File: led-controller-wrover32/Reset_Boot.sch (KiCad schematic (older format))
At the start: 8 parts, among them Q5 BSS138DW-7-F, SW1 SW_SPST_KMR2, SW2 SW_SPST_KMR2

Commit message: Cleanup
Signed-off-by: Aaron Williams <aaron.w2@gmail.com>
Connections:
- net ~RST_SW_OUT: now reaches C23.1, R3.1, RN6.2 (R2.1), RN6.3 (R3.1), RN6.4 (R4.1), SW2.2 (S1)
- net RST_IO2_DRV: now reaches Q5.2 (G2), RN6.7 (R2.2)
- net RST_IO0_DRV: now reaches Q5.5 (G1), RN6.6 (R3.2)
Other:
- moved on the sheet: Q5
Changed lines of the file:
@@
 EESchema Schematic File Version 4
-LIBS:led-controller-wrover32-cache
 EELAYER 30 0
 EELAYER END
 $Descr A4 11693 8268
 encoding utf-8
-Sheet 4 4
+Sheet 4 5
 Title ""
 Date ""
@@
 L dk_Transistors-FETs-MOSFETs-Arrays:BSS138DW-7-F Q5
 U 1 1 5DD66E94
-P 4800 2350
-F 0 "Q5" H 4750 2837 60  0000 C CNN
-F 1 "BSS138DW-7-F" H 4750 2731 60  0000 C CNN
-F 2 "Package_TO_SOT_SMD:SOT-363_SC-70-6" H 5000 2550 60  0001 L CNN
-F 3 "https://www.diodes.com/assets/Datasheets/ds30203.pdf" V 5000 2650 60  0001 L CNN
-F 4 "BSS138DW-FDICT-ND" H 5000 2750 60  0001 L CNN "Digi-Key_PN"
-F 5 "BSS138DW-7-F" H 5000 2850 60  0001 L CNN "MPN"
-F 6 "Discrete Semiconductor Products" H 5000 2950 60  0001 L CNN "Category"
-F 7 "Transistors - FETs, MOSFETs - Arrays" H 5000 3050 60  0001 L CNN "Family"
-F 8 "https://www.diodes.com/assets/Datasheets/ds30203.pdf" H 5000 3150 60  0001 L CNN "DK_Datasheet_Link"
-F 9 "/product-detail/en/diodes-incorporated/BSS138DW-7-F/BSS138DW-FDICT-ND/808541" H 5000 3250 60  0001 L CNN "DK_Detail_Page"
-F 10 "MOSFET 2N-CH 50V 0.2A SC70-6" H 5000 3350 60  0001 L CNN "Description"
-F 11 "Diodes Incorporated" H 5000 3450 60  0001 L CNN "Manufacturer"
-F 12 "Active" H 5000 3550 60  0001 L CNN "Status"
-F 13 "Diodes Incorporated" H 4800 2350 50  0001 C CNN "MFR"
-F 14 "Digikey" H 4800 2350 50  0001 C CNN "SPR"
-F 15 "BSS138DW-FDICT-ND" H 4800 2350 50  0001 C CNN "SPN"
-F 16 "https://www.digikey.com/products/en/discrete-semiconductor-products/transistors-fets-mosfets-arrays/289?k=BSS138DW-7-F&k=&pkeyword=BSS138DW-7-F&sv=0&pv7=2&sf=0&quantity=&ColumnSort=0&page=1&stock=1&nstock=1&pageSize=500" H 4800 2350 50  0001 C CNN "SPURL"
-	1    4800 2350
+P 5050 2350
+F 0 "Q5" H 5000 2837 60  0000 C CNN
+F 1 "BSS138DW-7-F" H 5000 2731 60  0000 C CNN
+F 2 "Package_TO_SOT_SMD:SOT-363_SC-70-6" H 5250 2550 60  0001 L CNN
+F 3 "https://www.diodes.com/assets/Datasheets/ds30203.pdf" V 5250 2650 60  0001 L CNN
+F 4 "BSS138DW-FDICT-ND" H 5250 2750 60  0001 L CNN "Digi-Key_PN"
+F 5 "BSS138DW-7-F" H 5250 2850 60  0001 L CNN "MPN"
+F 6 "Discrete Semiconductor Products" H 5250 2950 60  0001 L CNN "Category"
+F 7 "Transistors - FETs, MOSFETs - Arrays" H 5250 3050 60  0001 L CNN "Family"
+F 8 "https://www.diodes.com/assets/Datasheets/ds30203.pdf" H 5250 3150 60  0001 L CNN "DK_Datasheet_Link"
+F 9 "/product-detail/en/diodes-incorporated/BSS138DW-7-F/BSS138DW-FDICT-ND/808541" H 5250 3250 60  0001 L CNN "DK_Detail_Page"
+F 10 "MOSFET 2N-CH 50V 0.2A SC70-6" H 5250 3350 60  0001 L CNN "Description"
+F 11 "Diodes Incorporated" H 5250 3450 60  0001 L CNN "Manufacturer"
+F 12 "Active" H 5250 3550 60  0001 L CNN "Status"
+F 13 "Diodes Incorporated" H 5050 2350 50  0001 C CNN "MFR"
+F 14 "Digikey" H 5050 2350 50  0001 C CNN "SPR"
+F 15 "BSS138DW-FDICT-ND" H 5050 2350 50  0001 C CNN "SPN"
+F 16 "https://www.digikey.com/products/en/discrete-semiconductor-products/transistors-fets-mosfets-arrays/289?k=BSS138DW-7-F&k=&pkeyword=BSS138DW-7-F&sv=0&pv7=2&sf=0&quantity=&ColumnSort=0&page=1&stock=1&nstock=1&pageSize=500" H 5050 2350 50  0001 C CNN "SPURL"
+	1    5050 2350
 	1    0    0    -1
 $EndComp
@@
 $EndComp
 Wire Wire Line
-	4100 2450 4500 2450
+	4100 2450 4750 2450
 Wire Wire Line
 	4100 2350 4250 2350
@@
 	4250 2350 4250 1800
 Wire Wire Line
-	4250 1800 5200 1800
-Wire Wire Line
-	5200 1800 5200 2450
-Wire Wire Line
-	5200 2450 5000 2450
+	4250 1800 5450 1800
+Wire Wire Line
+	5450 1800 5450 2450
+Wire Wire Line
+	5450 2450 5250 2450
 $Comp
 L power:GND #PWR0127
 U 1 1 5DD73FDE
-P 4500 2150
-F 0 "#PWR0127" H 4500 1900 50  0001 C CNN
-F 1 "GND" H 4505 1977 50  0000 C CNN
-F 2 "" H 4500 2150 50  0001 C CNN
-F 3 "" H 4500 2150 50  0001 C CNN
-	1    4500 2150
+P 4750 2150
+F 0 "#PWR0127" H 4750 1900 50  0001 C CNN
+F 1 "GND" H 4755 1977 50  0000 C CNN
+F 2 "" H 4750 2150 50  0001 C CNN
+F 3 "" H 4750 2150 50  0001 C CNN
+	1    4750 2150
 	1    0    0    -1
 $EndComp
@@
 L power:GND #PWR0128
 U 1 1 5DD74502
-P 5000 2750
-F 0 "#PWR0128" H 5000 2500 50  0001 C CNN
-F 1 "GND" H 5005 2577 50  0000 C CNN
-F 2 "" H 5000 2750 50  0001 C CNN
-F 3 "" H 5000 2750 50  0001 C CNN
-	1    5000 2750
-	1    0    0    -1
-$EndComp
-Wire Wire Line
-	5000 2150 5650 2150
+P 5250 2750
+F 0 "#PWR0128" H 5250 2500 50  0001 C CNN
+F 1 "GND" H 5255 2577 50  0000 C CNN
+F 2 "" H 5250 2750 50  0001 C CNN
+F 3 "" H 5250 2750 50  0001 C CNN
+	1    5250 2750
+	1    0    0    -1
+$EndComp
+Wire Wire Line
+	5250 2150 5650 2150
 Text Label 5500 2150 0    50   ~ 0
 IO0
 Wire Wire Line
-	4500 2750 4500 3100
-Wire Wire Line
-	4500 3100 5650 3100
+	4750 2750 4750 3100
+Wire Wire Line
+	4750 3100 5650 3100
 Text Label 5500 3100 0    50   ~ 0
 IO2
@@
 NoConn ~ 4100 2250
 NoConn ~ 3700 2250
+Text Label 3200 2450 0    50   ~ 0
+~RST_SW_OUT
+Text Label 4450 1800 0    50   ~ 0
+RST_IO2_DRV
+Text Label 4150 2450 0    50   ~ 0
+RST_IO0_DRV
 $EndSCHEMATC

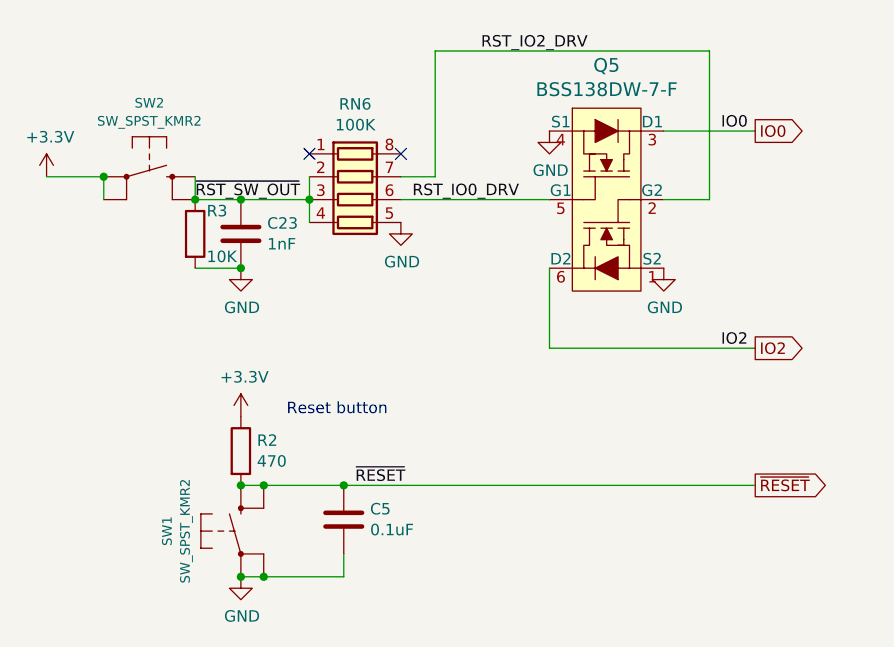
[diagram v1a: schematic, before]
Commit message: Fix reset circuit and other stuff
This fixes the reset circuit and moves a few components.  It also
cleans up the BOM a bit.

Also bumped to version 3.5.0

Signed-off-by: Aaron Williams <aaron.w2@gmail.com>
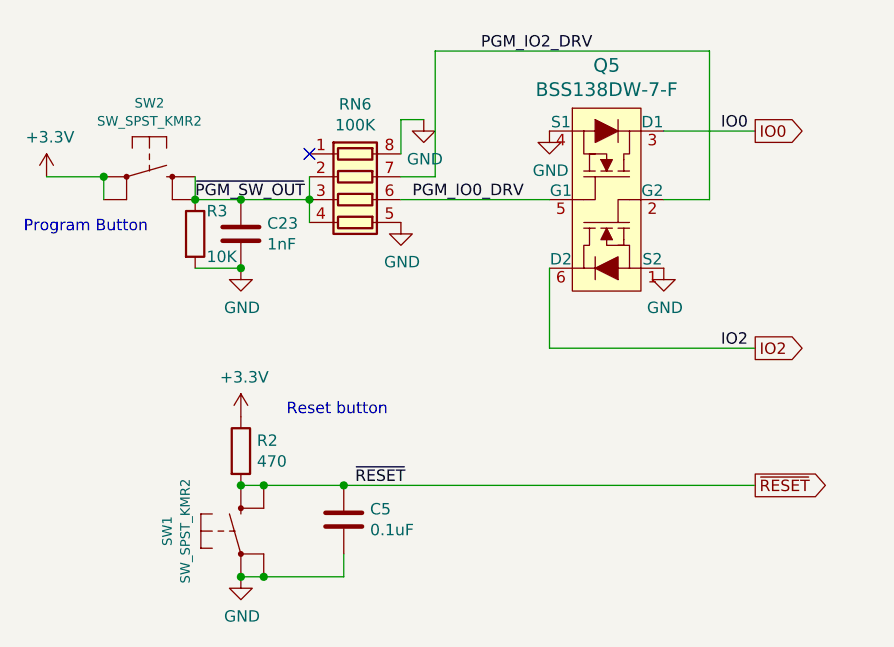
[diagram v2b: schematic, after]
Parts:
- R3: MFR (none) -> Vishay Dale; MPN (none) -> CRCW060310K0FKEC; SPN (none) -> 541-2979-1-ND; SPR (none) -> Digikey; SPURL (none) -> -
- RN6: MFR Bourns -> Panasonic; MPN CAT16-1003F4LF -> EXB-V8V103JV; SPN CAT16-1003F4LFCT-ND -> Y4103CT-ND
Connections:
- net GND: now also RN6.8 (R1.2)
- net RST_IO0_DRV renamed PGM_IO0_DRV
- net RST_IO2_DRV renamed PGM_IO2_DRV
- net ~RST_SW_OUT renamed ~PGM_SW_OUT
- no-connect marks 2 -> 1
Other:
- note added: "Program Button"

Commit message: Moved WS2813B after fixing footprint  v3.6
Signed-off-by: Aaron Williams <aaron.w2@gmail.com>
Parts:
- C23: value 1nF -> 22nF; MFR Kemet -> Yageo; MPN C0603C102K4RECAUTO -> CC0603JRX7R9BB223; SPN 399-17878-1-ND -> 311-4010-1-ND; SPURL https://www.digikey.com/product-detail/en/kemet/C0603C102K4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 -> https://www.digikey.com/product-detail/en/yageo/CC0603JRX7R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
- C5: MFR Samsung -> Murata Electronics; MPN CL10B104KO8WPNC -> GCM188R71H104KA57D; SPN 1276-6582-1-ND -> 490-4779-1-ND

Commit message: Minor changes
- Tweaked some of the component values in the 12V supply as per TI.
- Removed unnecessary protection diode, the USB one is enough.
- Changed UART to CS2104 which eliminates two resistors and is
  slightly cheaper
- Updated PCB to reflect changes.

Signed-off-by: Aaron Williams <aaron.w2@gmail.com>
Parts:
- C23: DESC (none) -> CAP CER 0.022UF 50V X7R 0603
- C5: DESC (none) -> CAP CER 0.1UF 50V X7R 0603
- Q5: DESC (none) -> MOSFET 2N-CH 50V 0.2A SC70-6
- R2: DESC (none) -> RES SMD 470 OHM 1% 1/10W 0603
- R3: DESC (none) -> RES SMD 10K OHM 1% 1/10W 0603
- RN6: DESC (none) -> RES ARRAY 4 RES 100K OHM 1206; MPN EXB-V8V103JV -> EXB-V8V104JV; SPN Y4103CT-ND -> Y4104CT-ND
- SW1, SW2: DESC (none) -> SWITCH TACTILE SPST-NO 0.05A 32V
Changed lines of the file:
@@
 F 15 "BSS138DW-FDICT-ND" H 5050 2350 50  0001 C CNN "SPN"
 F 16 "https://www.digikey.com/products/en/discrete-semiconductor-products/transistors-fets-mosfets-arrays/289?k=BSS138DW-7-F&k=&pkeyword=BSS138DW-7-F&sv=0&pv7=2&sf=0&quantity=&ColumnSort=0&page=1&stock=1&nstock=1&pageSize=500" H 5050 2350 50  0001 C CNN "SPURL"
+F 17 "MOSFET 2N-CH 50V 0.2A SC70-6" H 0   0   50  0001 C CNN "DESC"
 	1    5050 2350
 	1    0    0    -1
@@
 F 7 "401-1426-1-ND" H 3000 2350 50  0001 C CNN "SPN"
 F 8 "https://www.digikey.com/product-detail/en/c-k/KMR211GLFS/401-1426-1-ND/550461" H 3000 2350 50  0001 C CNN "SPURL"
+F 9 "SWITCH TACTILE SPST-NO 0.05A 32V" H 0   0   50  0001 C CNN "DESC"
 	1    3000 2350
 	1    0    0    -1
@@
 F 3 "https://industrial.panasonic.com/cdbs/www-data/pdf/AOC0000/AOC0000C14.pdf" H 3900 2450 50  0001 C CNN
 F 4 "Panasonic" H 3900 2450 50  0001 C CNN "MFR"
-F 5 "EXB-V8V103JV" H 3900 2450 50  0001 C CNN "MPN"
+F 5 "EXB-V8V104JV" H 3900 2450 50  0001 C CNN "MPN"
 F 6 "Digikey" H 3900 2450 50  0001 C CNN "SPR"
-F 7 "Y4103CT-ND" H 3900 2450 50  0001 C CNN "SPN"
+F 7 "Y4104CT-ND" H 3900 2450 50  0001 C CNN "SPN"
 F 8 "https://www.digikey.com/product-detail/en/bourns-inc/CAT16-1003F4LF/CAT16-1003F4LFCT-ND/3592894" H 3900 2450 50  0001 C CNN "SPURL"
+F 9 "RES ARRAY 4 RES 100K OHM 1206" H 0   0   50  0001 C CNN "DESC"
 	1    3900 2450
 	0    1    1    0
@@
 F 7 "1276-4619-1-ND" H -1100 2500 50  0001 C CNN "SPN"
 F 8 "-" H -1100 2500 50  0001 C CNN "SPURL"
+F 9 "RES SMD 470 OHM 1% 1/10W 0603" H 0   0   50  0001 C CNN "DESC"
 	1    3400 3550
 	1    0    0    -1
@@
 F 7 "490-4779-1-ND" H -1100 2300 50  0001 C CNN "SPN"
 F 8 "-" H -1100 2300 50  0001 C CNN "SPURL"
+F 9 "CAP CER 0.1UF 50V X7R 0603" H 0   0   50  0001 C CNN "DESC"
 	1    3850 3850
 	1    0    0    -1
@@
 F 7 "401-1426-1-ND" H 3400 3900 50  0001 C CNN "SPN"
 F 8 "https://www.digikey.com/product-detail/en/c-k/KMR211GLFS/401-1426-1-ND/550461" H 3400 3900 50  0001 C CNN "SPURL"
+F 9 "SWITCH TACTILE SPST-NO 0.05A 32V" H 0   0   50  0001 C CNN "DESC"
 	1    3400 3900
 	0    -1   -1   0
@@
 F 7 "541-2979-1-ND" H 0   0   50  0001 C CNN "SPN"
 F 8 "-" H 0   0   50  0001 C CNN "SPURL"
+F 9 "RES SMD 10K OHM 1% 1/10W 0603" H 0   0   50  0001 C CNN "DESC"
 	1    3200 2600
 	1    0    0    -1
@@
 F 7 "311-4010-1-ND" H 3400 2600 50  0001 C CNN "SPN"
 F 8 "https://www.digikey.com/product-detail/en/yageo/CC0603JRX7R9BB223/311-4010-1-ND/8025099" H 3400 2600 50  0001 C CNN "SPURL"
+F 9 "CAP CER 0.022UF 50V X7R 0603" H 0   0   50  0001 C CNN "DESC"
 	1    3400 2600
 	1    0    0    -1
